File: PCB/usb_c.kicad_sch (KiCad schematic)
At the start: 3 parts

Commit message: refactor: erc is clean
This gets the schematic as clean as it can be.
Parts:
- removed J_USB: USB-C, symbol Connector:USB_C_Receptacle_USB2.0_16P
- added J_USB1: USB-C, symbol Connector:USB_C_Receptacle_USB2.0_16P
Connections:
- net GND: now also J_USB1.A1 (GND), J_USB1.A12 (GND), J_USB1.B1 (GND), J_USB1.B12 (GND), J_USB1.S1 (SHIELD)
- net USB_CC1: now also J_USB1.A5 (CC1)
- net USB_CC2: now also J_USB1.B5 (CC2)
- net USB_DM: now also J_USB1.A7 (D-), J_USB1.B7 (D-)
- net USB_DP: now also J_USB1.A6 (D+), J_USB1.B6 (D+)
- net VBUS: now also J_USB1.A4 (VBUS), J_USB1.A9 (VBUS), J_USB1.B4 (VBUS), J_USB1.B9 (VBUS)
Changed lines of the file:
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@@
+	)
+	(label "USB_CC2"
+		(at 163.83 100.33 0)
+		(effects
+			(font
+				(size 1.27 1.27)
+			)
+			(justify left)
+		)
 	)
 	(label "USB_CC2"
@@
 	)
 	(label "USB_CC1"
+		(at 163.83 97.79 0)
+		(effects
+			(font
+				(size 1.27 1.27)
+			)
+			(justify left)
+		)
+	)
+	(label "USB_CC1"
 		(at 105.41 97.79 90)
 		(effects
@@
 		)
 	)
-	(label "USB_CC2"
-		(at 163.83 100.33 0)
-		(effects
-			(font
-				(size 1.27 1.27)
-			)
-			(justify left)
-		)
-	)
-	(label "USB_CC1"
-		(at 163.83 97.79 0)
-		(effects
-			(font
-				(size 1.27 1.27)
-			)
-			(justify left)
-		)
-	)
-	(global_label "GND"
-		(shape passive)
-		(at 148.59 130.81 270)
-		(fields_autoplaced yes)
-		(effects
-			(font
-				(size 1.27 1.27)
-			)
-			(justify right)
-		)
-		(property "Intersheetrefs" "${INTERSHEET_REFS}"
-			(at 148.59 130.81 0)
-			(effects
-				(font
-					(size 1.27 1.27)
-				)
-				(hide yes)
-			)
-		)
-	)
 	(global_label "GND"
 		(shape passive)
@@
 	(global_label "GND"
 		(shape passive)
-		(at 148.59 130.81 270)
-		(fields_autoplaced yes)
-		(effects
-			(font
-				(size 1.27 1.27)
-			)
-			(justify right)
-		)
-		(property "Intersheetrefs" "${INTERSHEET_REFS}"
-			(at 148.59 130.81 0)
-			(effects
-				(font
-					(size 1.27 1.27)
-				)
-				(hide yes)
-			)
-		)
-	)
-	(global_label "GND"
-		(shape passive)
-		(at 105.41 105.41 270)
-		(fields_autoplaced yes)
-		(effects
-			(font
-				(size 1.27 1.27)
-			)
-			(justify right)
-		)
-		(property "Intersheetrefs" "${INTERSHEET_REFS}"
-			(at 105.41 105.41 0)
+		(at 191.77 105.41 270)
+		(fields_autoplaced yes)
+		(effects
+			(font
+				(size 1.27 1.27)
+			)
+			(justify right)
+		)
+		(property "Intersheetrefs" "${INTERSHEET_REFS}"
+			(at 191.77 105.41 0)
 			(effects
 				(font
@@
 	(global_label "GND"
 		(shape passive)
-		(at 191.77 105.41 270)
-		(fields_autoplaced yes)
-		(effects
-			(font
-				(size 1.27 1.27)
-			)
-			(justify right)
-		)
-		(property "Intersheetrefs" "${INTERSHEET_REFS}"
-			(at 191.77 105.41 0)
+		(at 148.59 130.81 270)
+		(fields_autoplaced yes)
+		(effects
+			(font
+				(size 1.27 1.27)
+			)
+			(justify right)
+		)
+		(property "Intersheetrefs" "${INTERSHEET_REFS}"
+			(at 148.59 130.81 0)
+			(effects
+				(font
+					(size 1.27 1.27)
+				)
+				(hide yes)
+			)
+		)
+	)
+	(global_label "GND"
+		(shape passive)
+		(at 148.59 130.81 270)
+		(fields_autoplaced yes)
+		(effects
+			(font
+				(size 1.27 1.27)
+			)
+			(justify right)
+		)
+		(property "Intersheetrefs" "${INTERSHEET_REFS}"
+			(at 148.59 130.81 0)
 			(effects
 				(font
@@
 		)
 	)
+	(global_label "GND"
+		(shape passive)
+		(at 148.59 130.81 270)
+		(fields_autoplaced yes)
+		(effects
+			(font
+				(size 1.27 1.27)
+			)
+			(justify right)
+		)
+		(property "Intersheetrefs" "${INTERSHEET_REFS}"
+			(at 148.59 130.81 0)
+			(effects
+				(font
+					(size 1.27 1.27)
+				)
+				(hide yes)
+			)
+		)
+	)
+	(global_label "GND"
+		(shape passive)
+		(at 105.41 105.41 270)
+		(fields_autoplaced yes)
+		(effects
+			(font
+				(size 1.27 1.27)
+			)
+			(justify right)
+		)
+		(property "Intersheetrefs" "${INTERSHEET_REFS}"
+			(at 105.41 105.41 0)
+			(effects
+				(font
+					(size 1.27 1.27)
+				)
+				(hide yes)
+			)
+		)
+	)
 	(global_label "VBUS"
 		(shape input)
@@
 		)
 	)
-	(global_label "GND"
-		(shape passive)
-		(at 148.59 130.81 270)
-		(fields_autoplaced yes)
-		(effects
-			(font
-				(size 1.27 1.27)
-			)
-			(justify right)
-		)
-		(property "Intersheetrefs" "${INTERSHEET_REFS}"
-			(at 148.59 130.81 0)
-			(effects
-				(font
-					(size 1.27 1.27)
-				)
-				(hide yes)
-			)
-		)
-	)
 	(hierarchical_label "USB_DM"
 		(shape bidirectional)
@@
 			)
 			(justify left)
+		)
+	)
+	(symbol
+		(lib_id "Device:R")
+		(at 191.77 101.6 0)
+		(unit 1)
+		(exclude_from_sim no)
+		(in_bom yes)
+		(on_board yes)
+		(dnp no)
+		(fields_autoplaced yes)
+		(property "Reference" "R_CC2"
+			(at 193.802 101.6 90)
+			(effects
+				(font
+					(size 1.27 1.27)
+				)
+			)
+		)
+		(property "Value" "5.1kΩ"
+			(at 191.77 101.6 90)
+			(effects
+				(font
+					(size 1.27 1.27)
+				)
+			)
+		)
+		(property "Footprint" ""
+			(at 189.992 101.6 90)
+			(effects
+				(font
+					(size 1.27 1.27)
+				)
+				(hide yes)
+			)
+		)
+		(property "Datasheet" "~"
+			(at 191.77 101.6 0)
+			(effects
+				(font
+					(size 1.27 1.27)
+				)
+				(hide yes)
+			)
+		)
+		(property "Description" "Resistor"
+			(at 191.77 101.6 0)
+			(effects
+				(font
+					(size 1.27 1.27)
+				)
+				(hide yes)
+			)
+		)
+		(pin "1"
+		)
+		(pin "2"
+		)
+		(instances
+			(project "snips_controller"
+				(path "/70589bdd-acbd-4920-8e78-aa58d10832b9/2c2b3d28-8ac2-4987-8c53-96e65f7bf4f4"
+					(reference "R_CC2")
+					(unit 1)
+				)
+			)
 		)
 	)
@@
 		(dnp no)
 		(fields_autoplaced yes)
-		(property "Reference" "J_USB"
+		(property "Reference" "J_USB1"
 			(at 148.59 130.175 0)
 			(effects
@@
 		(instances
 			(project "snips_controller"
-				(path "/2289c08f-f540-4e27-86fd-a28b71d1d149/89b20f31-77e1-4703-939a-baaa45dd618e"
-					(reference "J_USB")
-					(unit 1)
-				)
-			)
-		)
-	)
-	(symbol
-		(lib_id "Device:R")
-		(at 191.77 101.6 0)
-		(unit 1)
-		(exclude_from_sim no)
-		(in_bom yes)
-		(on_board yes)
-		(dnp no)
-		(fields_autoplaced yes)
-		(property "Reference" "R_CC2"
-			(at 193.802 101.6 90)
-			(effects
-				(font
-					(size 1.27 1.27)
-				)
-			)
-		)
-		(property "Value" "5.1kΩ"
-			(at 191.77 101.6 90)
-			(effects
-				(font
-					(size 1.27 1.27)
-				)
-			)
-		)
-		(property "Footprint" ""
-			(at 189.992 101.6 90)
-			(effects
-				(font
-					(size 1.27 1.27)
-				)
-				(hide yes)
-			)
-		)
-		(property "Datasheet" "~"
-			(at 191.77 101.6 0)
-			(effects
-				(font
-					(size 1.27 1.27)
-				)
-				(hide yes)
-			)
-		)
-		(property "Description" "Resistor"
-			(at 191.77 101.6 0)
-			(effects
-				(font
-					(size 1.27 1.27)
-				)
-				(hide yes)
-			)
-		)
-		(pin "1"
-		)
-		(pin "2"
-		)
-		(instances
-			(project "snips_controller"
-				(path "/2289c08f-f540-4e27-86fd-a28b71d1d149/89b20f31-77e1-4703-939a-baaa45dd618e"
-					(reference "R_CC2")
+				(path "/70589bdd-acbd-4920-8e78-aa58d10832b9/2c2b3d28-8ac2-4987-8c53-96e65f7bf4f4"
+					(reference "J_USB1")
 					(unit 1)
 				)
@@
 		(instances
 			(project "snips_controller"
-				(path "/2289c08f-f540-4e27-86fd-a28b71d1d149/89b20f31-77e1-4703-939a-baaa45dd618e"
+				(path "/70589bdd-acbd-4920-8e78-aa58d10832b9/2c2b3d28-8ac2-4987-8c53-96e65f7bf4f4"
 					(reference "R_CC1")
 					(unit 1)

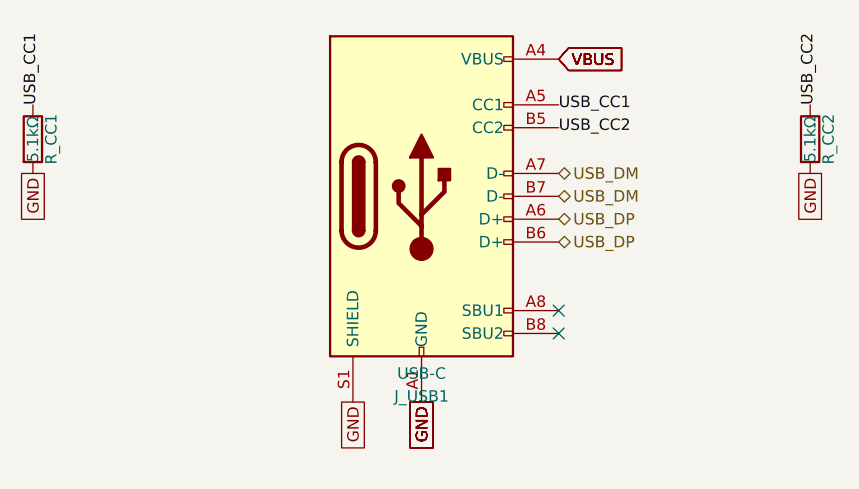
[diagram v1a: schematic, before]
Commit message: refactor: switch over to esp32-s3-wroom1 (#13)
This refactors to the esp32-s3 to avoid every problem we encountered with the raspberry pi options.
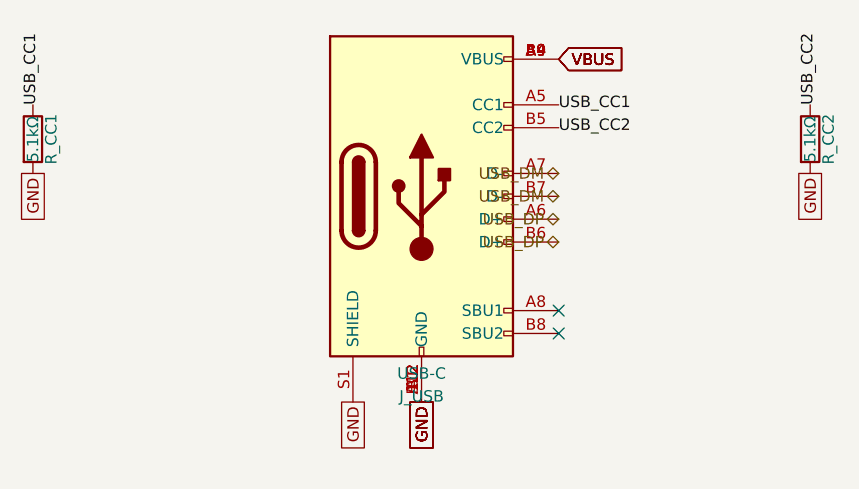
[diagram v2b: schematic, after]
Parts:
- removed J_USB1: USB-C, symbol Connector:USB_C_Receptacle_USB2.0_16P
- added J_USB: USB-C, Connector_USB:USB_C_Receptacle_HRO_TYPE-C-31-M-12, symbol Connector:USB_C_Receptacle_USB2.0_16P
- R_CC1, R_CC2: footprint (none) -> Resistor_SMD:R_0402_1005Metric
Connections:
- net GND: now also J_USB.A1 (GND), J_USB.A12 (GND), J_USB.B1 (GND), J_USB.B12 (GND), J_USB.S1 (SHIELD)
- net USB_CC1: now also J_USB.A5 (CC1)
- net USB_CC2: now also J_USB.B5 (CC2)
- net USB_DM: now also J_USB.A7 (D-), J_USB.B7 (D-)
- net USB_DP: now also J_USB.A6 (D+), J_USB.B6 (D+)
- net VBUS: now also J_USB.A4 (VBUS), J_USB.A9 (VBUS), J_USB.B4 (VBUS), J_USB.B9 (VBUS)

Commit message: cleanup: annotations and library updates
This is just a task to update the kicad libraries and annotations internally to get that clean ERC.
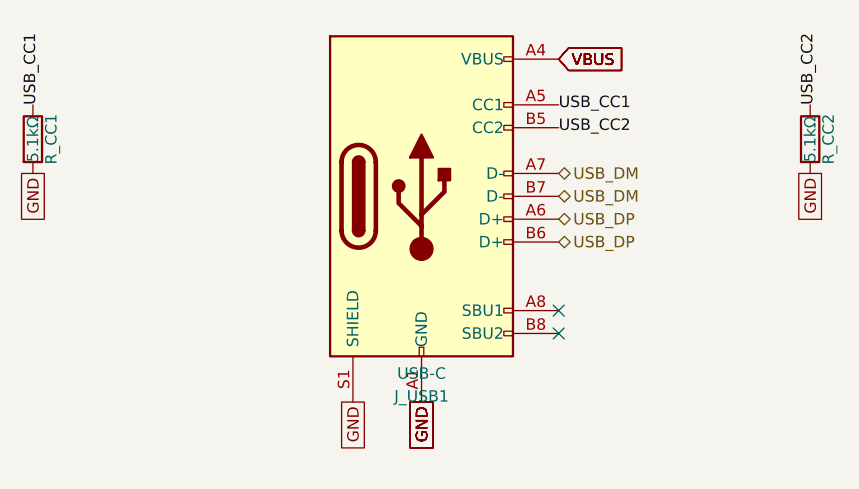
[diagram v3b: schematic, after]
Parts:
- renumbered J_USB to J_USB1
